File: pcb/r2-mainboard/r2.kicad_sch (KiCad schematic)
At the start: 0 parts

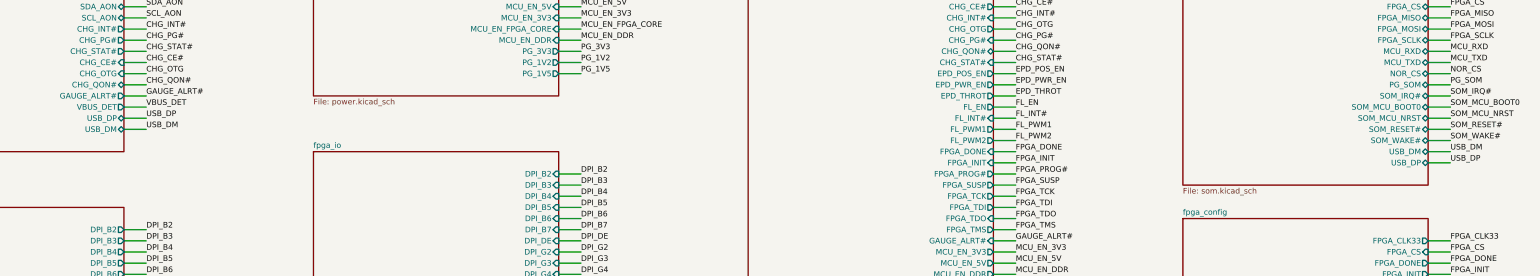
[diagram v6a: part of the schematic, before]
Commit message: R2: withdraw the RWU0007A thermal-pad concern -- it was wrong
power.md §7 item 2 said KiCad's Texas_RWU0007A_VQFN-7_2x2mm_P0.5mm leaves the
thermal-pad segments unnumbered, so U12's heat path is not tied to GND, and to
copy the footprint into r2.pretty and renumber those pads 1 before layout.

Reading the placed footprint with the layer field visible: the six unnumbered
pads are F.Paste ONLY. They are stencil apertures -- each large pad split into
two openings to control solder volume, the standard idiom at that size. Pads
1/2/3 are F.Cu + F.Mask, numbered, and netted GND / SW / +5V_DCDC. Pin 1 is the
thermal path per Table 5-1 and it is on GND already.

Acting on the note would have renumbered paste apertures into copper and
shorted GND, SW and VOUT together -- creating the failure it was meant to
prevent. Found because the owner is routing U12 right now.

§11.2 item 5 amended to a plain layout instruction, and §8's open-items list
no longer carries it.

Co-Authored-By: Claude Opus 5 <noreply@anthropic.com>
Claude-Session: https://claude.ai/code/session_01MnesETWABbVdbcVnCKfKVs
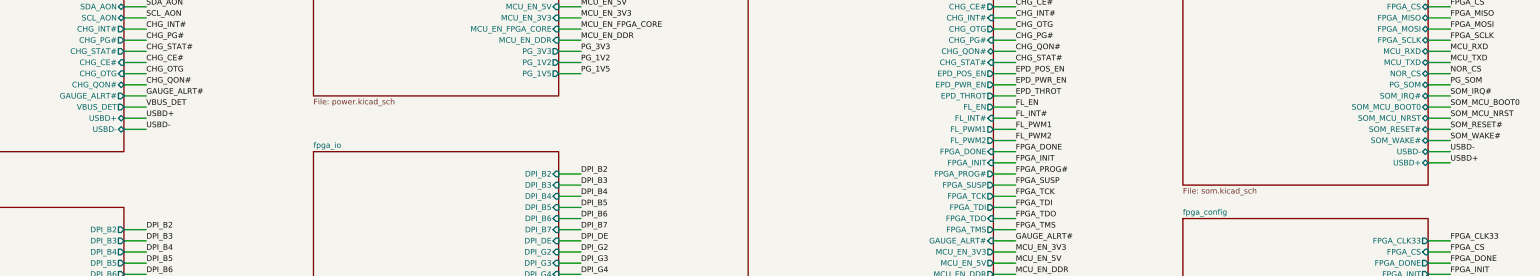
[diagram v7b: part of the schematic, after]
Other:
- sheet battery ports: added USBD+, USBD-; removed USB_DM, USB_DP
- sheet som ports: added USBD+, USBD-; removed USB_DM, USB_DP
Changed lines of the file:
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@@
 		)
 	)
-	(label "USB_DP"
+	(label "USBD+"
 		(at 83.82 60.96 0)
 		(effects
@@
 		)
 	)
-	(label "USB_DM"
+	(label "USBD-"
 		(at 381 68.58 0)
 		(effects
@@
 		)
 	)
-	(label "USB_DP"
+	(label "USBD+"
 		(at 381 71.12 0)
 		(effects
@@
 		)
 	)
-	(label "USB_DM"
+	(label "USBD-"
 		(at 83.82 63.5 0)
 		(effects
@@
 			)
 		)
-		(pin "USB_DM" bidirectional
+		(pin "USBD-" bidirectional
 			(at 375.92 68.58 0)
 			(effects
@@
 			)
 		)
-		(pin "USB_DP" bidirectional
+		(pin "USBD+" bidirectional
 			(at 375.92 71.12 0)
 			(effects
@@
 			)
 		)
-		(pin "USB_DP" bidirectional
+		(pin "USBD+" bidirectional
 			(at 78.74 60.96 0)
 			(effects
@@
 			)
 		)
-		(pin "USB_DM" bidirectional
+		(pin "USBD-" bidirectional
 			(at 78.74 63.5 0)
 			(effects
